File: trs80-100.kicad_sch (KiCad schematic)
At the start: 385 parts, among them CN2 A-7224, CN3 TCS-4480, CN4 TCS-4490, CN5 PRINTER CONNECTOR, CN6 RS232C, CN7 LCD-CONN, CN8 LCD-LED-CONN, J1 Adapter Jack CN9, K1 Key_Board, M1 40H373, M10 SystemBus, M11 ROM32k, M12 ROM32k, M13 40H032, M14 40H175, M15 40H244, M16 40H138, M17 40H000, M18 μPD1990AC, M19 80C85, M2 40H245, M20 40H367, M21 40H244, M22 IM6402, M23 40H244, M24 40H032, M25 81C55, M26 40H002, M27 4011, M28 4013, M29 TL064, M3 40H138, M30 TL064, M31 MC14412, M32 40H244, M33 40H157, M34 4584, M35 4584, M36 4013, M4 40H138, M5 40H139, M6 OPTION RAM #3, M7 OPTION RAM #2, M8 OPTION RAM #1, M9 STANDARD RAM, SW1 SSP32201, SW2 SSB34204, SW3 SLB-22BP-03, SW4 Reset Switch, SW5 SSP32201, T1 2SA1115, T10 2SC2603, T11 2SC2603, T13 2SC2603, T14 2SC2603(E), T15 2SC2603(E), T16 2SC2603(E), T17 2SC2603(E), T18 2SC2603, T19 2SA1115, T2 2SC2603, T20 2SC2603, T21 2SC2603(E), T22 2SC2603(E), T23 2SC2603, T24 2SC2603, T25 2SC2603, T27 2SC2603, T28 2SA1115, T3 2SC2603, T4 2SC2603, T5 2SC2603, T6 2SC2603, T7 2SC2603, T8 2SC2603, T9 2SC2603, X1 32.768kHz, X2 4.9152MHz, X3 1.0MHz

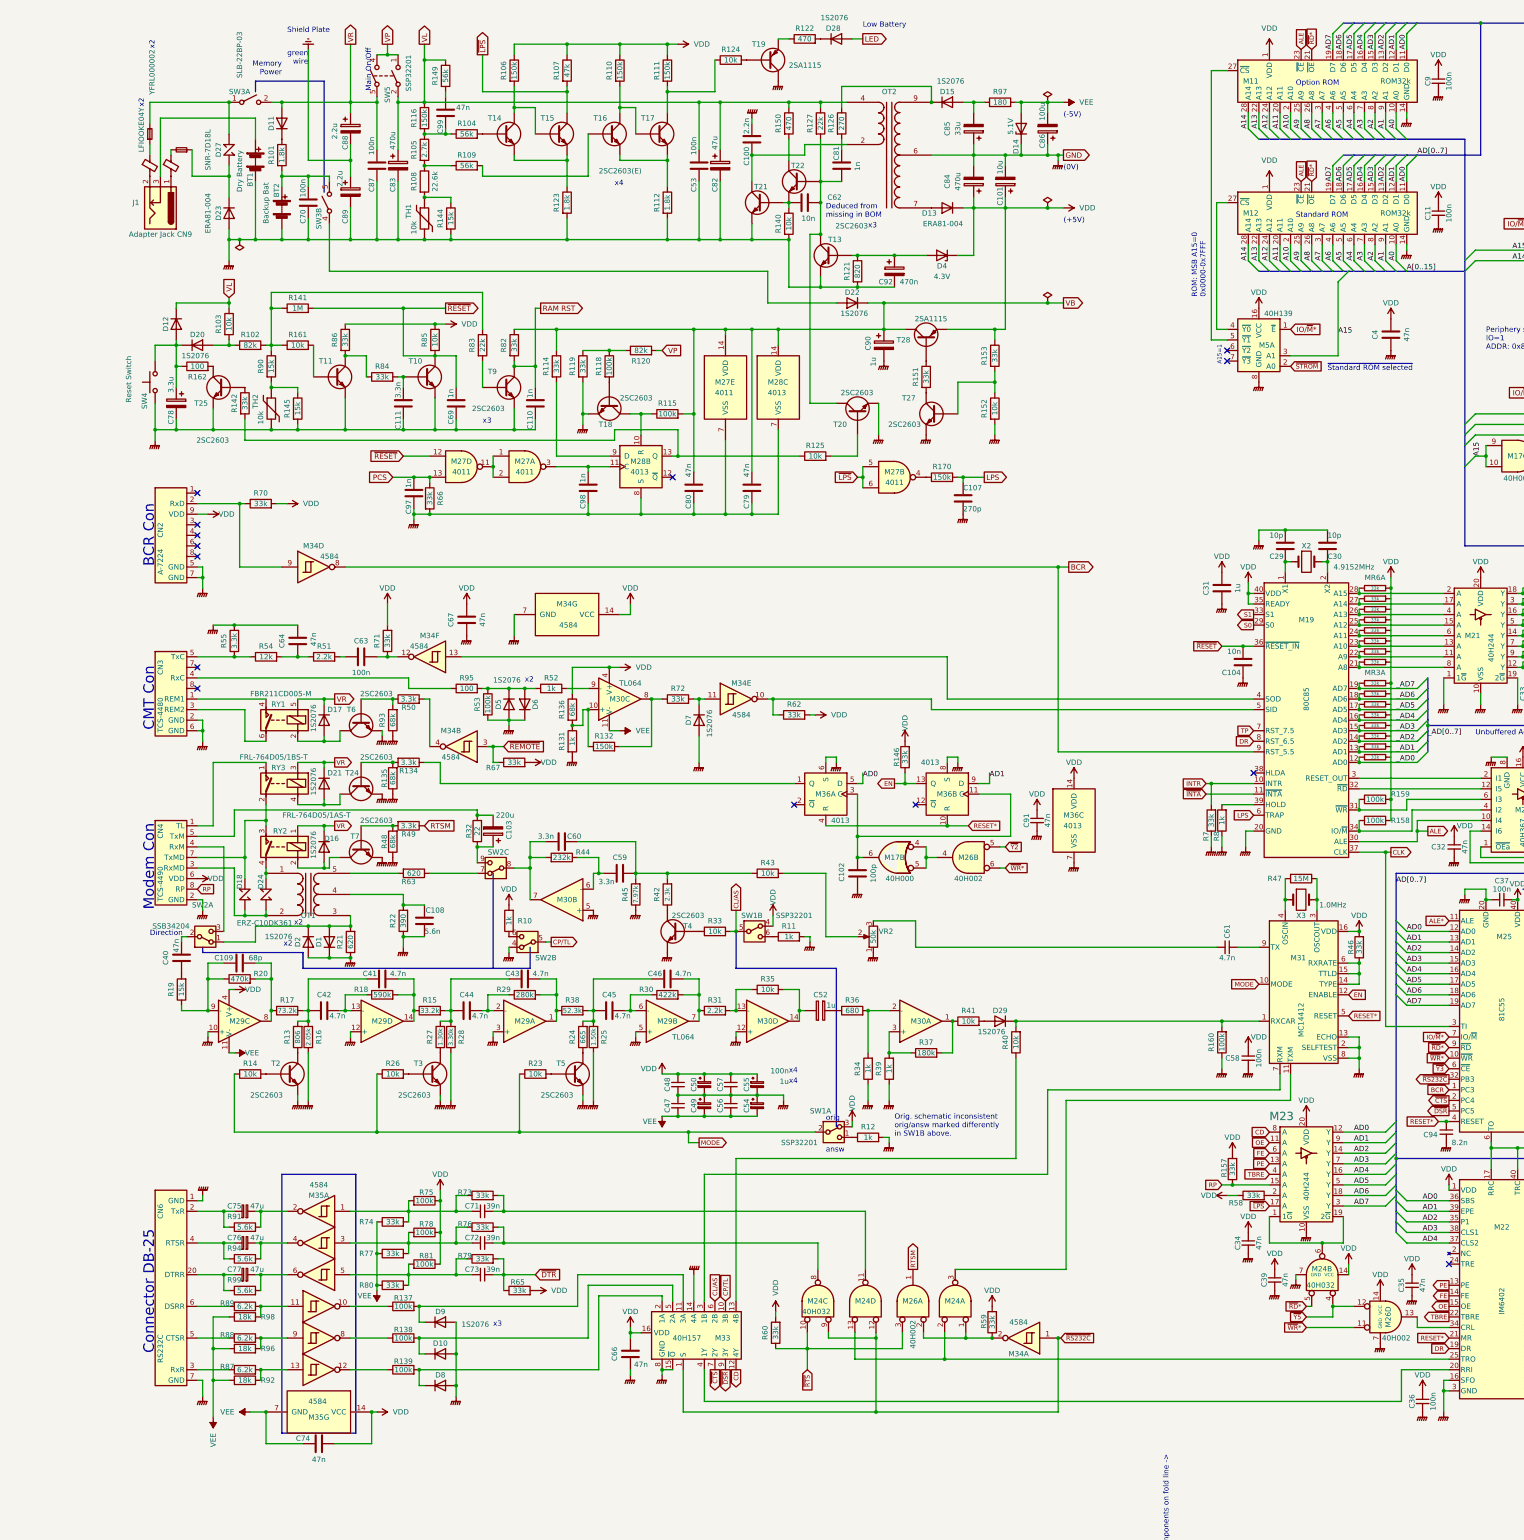
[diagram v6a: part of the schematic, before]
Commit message: Further free space around the fold line. Add labels for easy wire matching.
Provide more space around the center line to allow for easy folding
or printing in two parts without loosing important information.

Label the wires that go across the page halfs on both sides so that
they can be easily be matched.
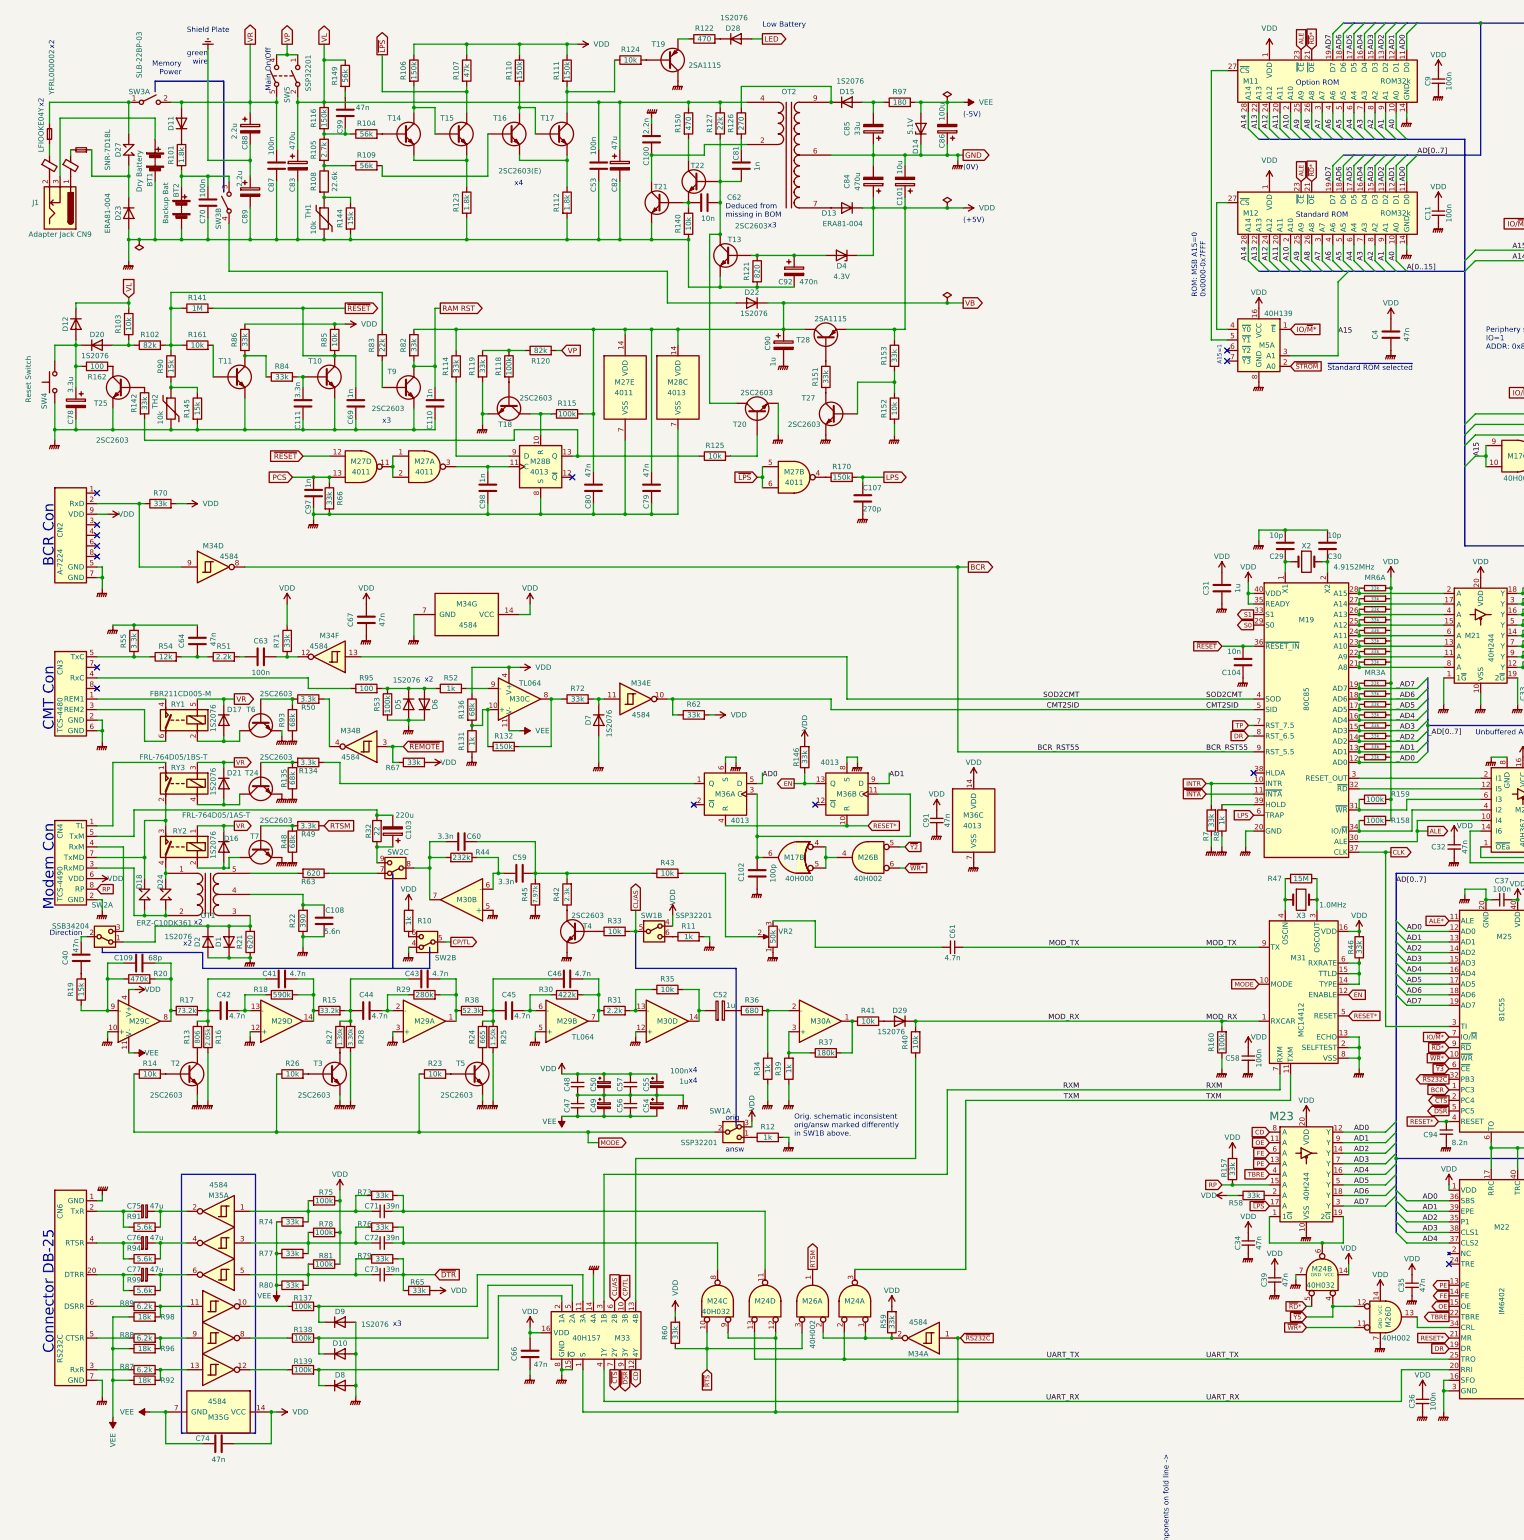
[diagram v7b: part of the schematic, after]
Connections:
- net UART_TX: now reaches M22.25 (TRO), M24.13, M24.2
- net SOD2CMT: now reaches M19.4 (SOD), M34.13
- net MOD_RX: now reaches D29.1 (K), M31.1 (RXCAR), R160.2, R40.2
- net TXM: now reaches M24.3, M31.11 (TXM)
- net RXM: now reaches M31.7 (RXM), M33.3 (1B)
- net MOD_TX: now reaches C61.1, M31.9 (TX)
- net CMT2SID: now reaches M19.5 (SID), M34.10, R62.1
- net UART_RX: now reaches M22.20 (RRI), M33.4 (1Y)
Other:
- moved on the sheet: BT1, BT2, C100, C101, C102, C103, C107, C108, C109, C110, C111, C40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
